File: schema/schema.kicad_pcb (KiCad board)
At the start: 2 copper layers, 91.4 x 55.9 mm, 14 parts, among them J1 Conn_01x04_Male, J2 Conn_01x04_Male, J3 Conn_01x05_Male

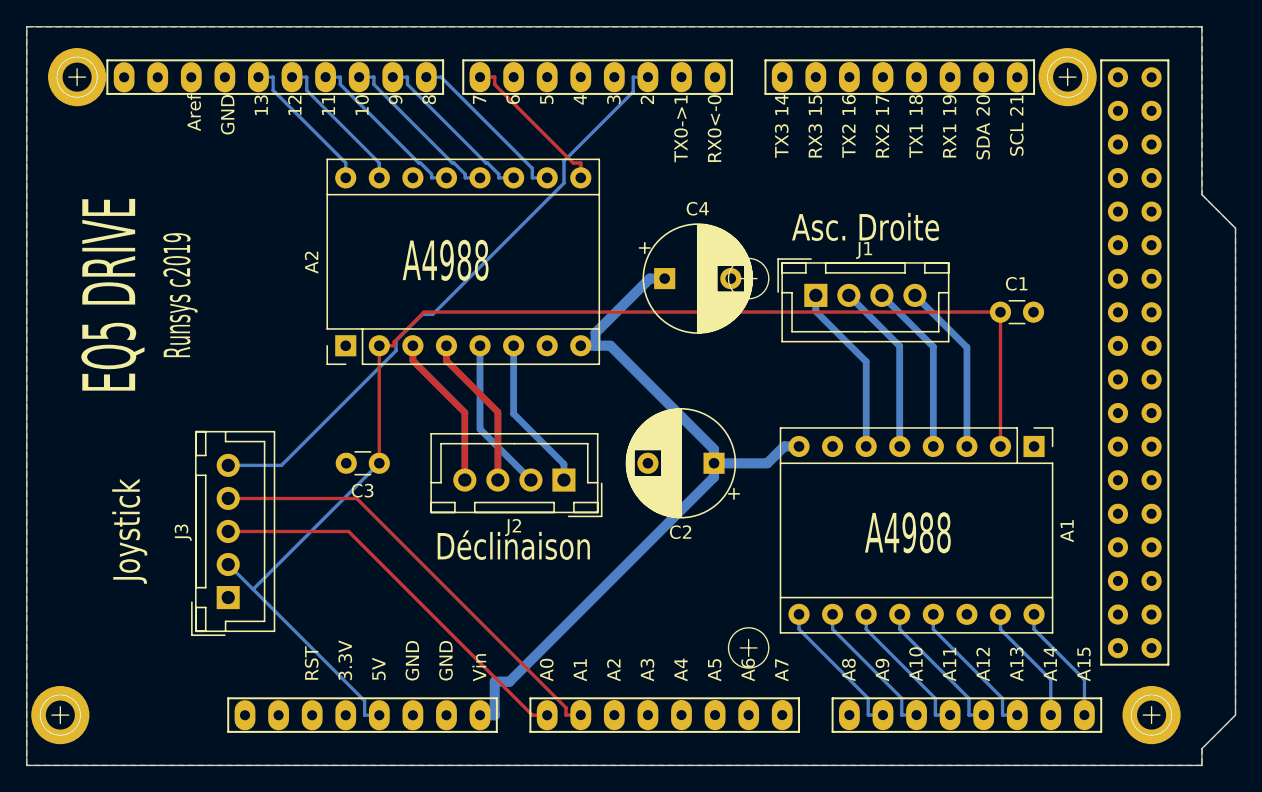
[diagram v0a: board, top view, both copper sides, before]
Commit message: Ajout Logo telescope
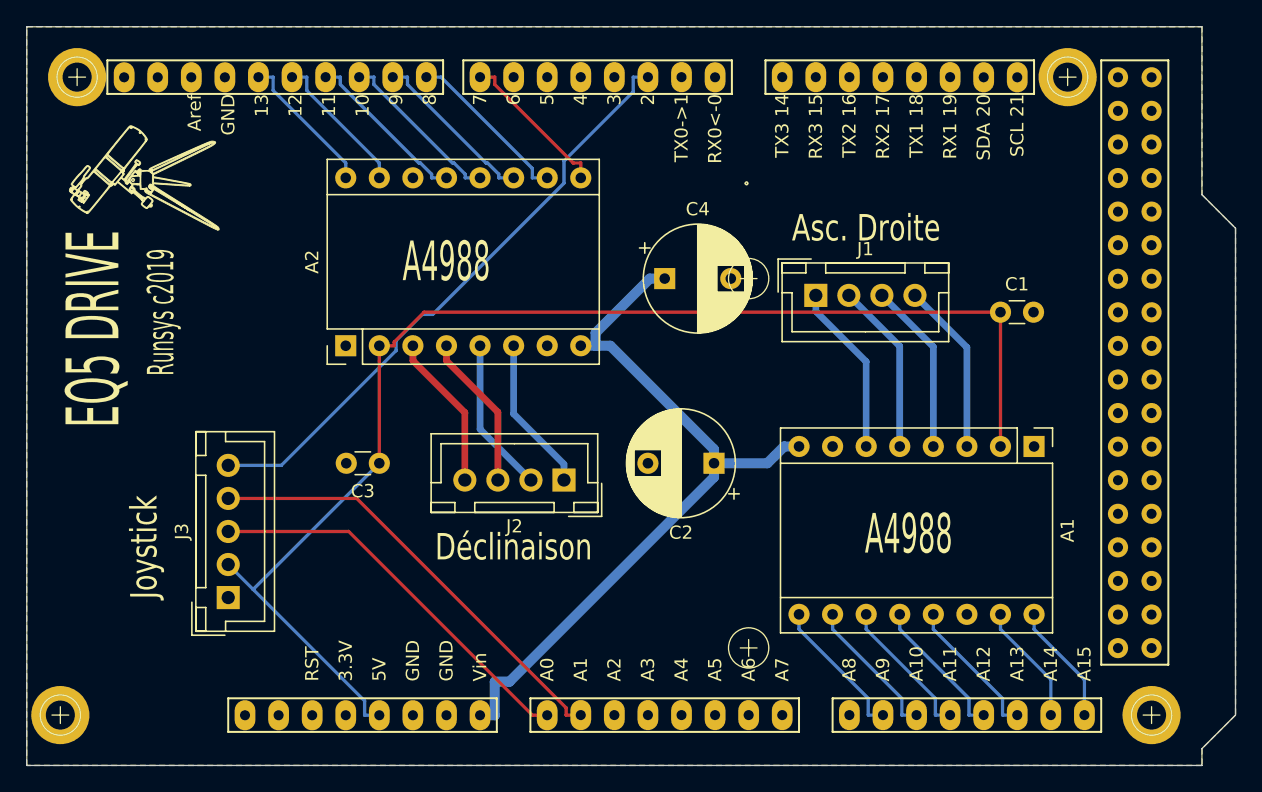
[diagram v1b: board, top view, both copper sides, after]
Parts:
- added G***: LOGO, logo:tele, F.Cu at (146.1, 74.9)
- added G***: LOGO, logo:tele, F.Cu at (100.3, 73.7)

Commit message: Modifiction du condo de 100nF
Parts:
- C1, C3: footprint Capacitors_THT:C_Disc_D3.0mm_W1.6mm_P2.50mm -> Capacitor_THT:C_Disc_D5.1mm_W3.2mm_P5.00mm
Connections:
- SH1 pad GND3: Net-(SH1-PadGND3) -> GND

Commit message: Modificatin pour la 3D sur les connexteurs JST
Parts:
- J1, J2: footprint Connectors_JST:JST_XH_B04B-XH-A_04x2.50mm_Straight -> Connector_JST:JST_XH_B4B-XH-A_1x04_P2.50mm_Vertical
- J3: footprint Connectors_JST:JST_XH_B05B-XH-A_05x2.50mm_Straight -> Connector_JST:JST_XH_B5B-XH-A_1x05_P2.50mm_Vertical

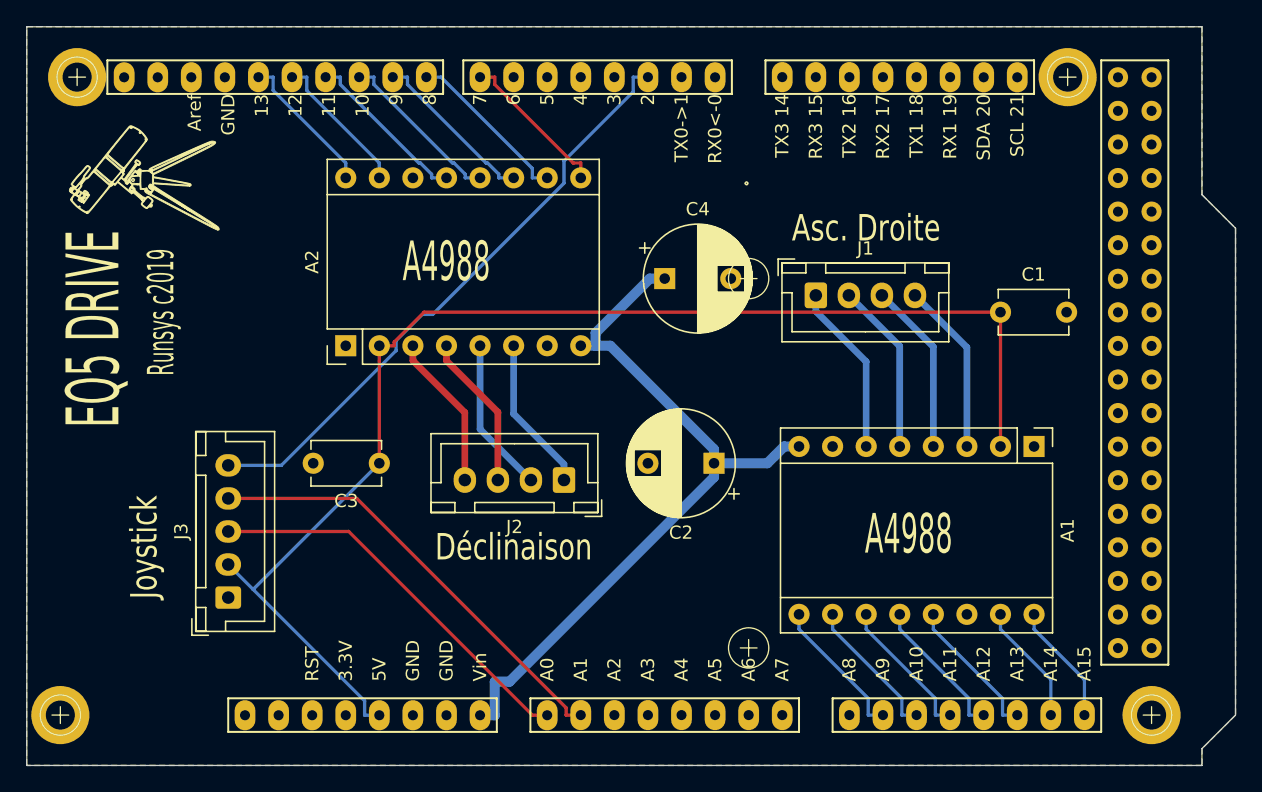
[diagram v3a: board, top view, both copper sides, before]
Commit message: Changement de taille des pistes 12V et 5V
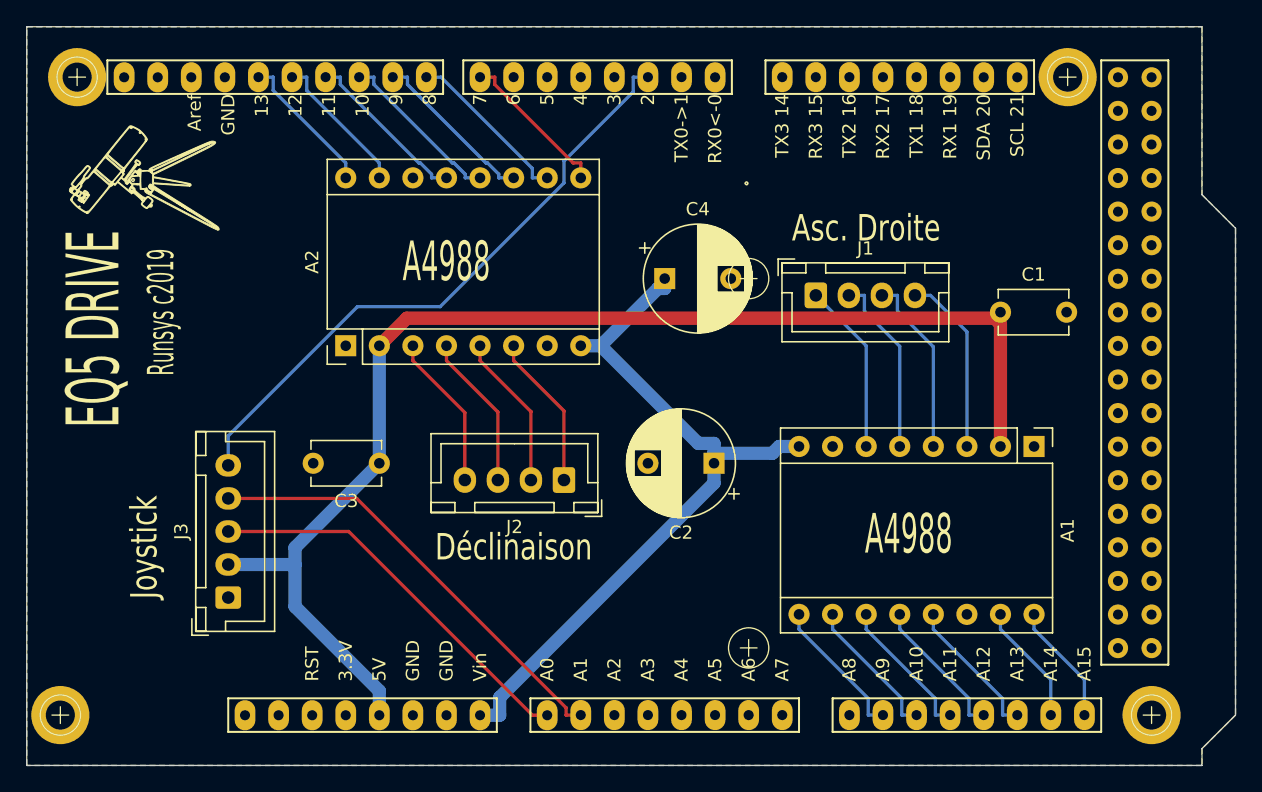
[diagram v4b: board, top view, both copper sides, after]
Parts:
- renumbered G*** to G0, G*** to G1, REF** to REF1, REF** to REF2, REF** to REF3
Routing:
- net +5V: track 97.5 -> 96.2 mm
- net +12V: track 56.9 -> 55.9 mm
- net Net-(J3-Pad5): track 46.0 -> 46.8 mm
- net Net-(A1-Pad5): track 13.0 -> 13.7 mm
- net Net-(A1-Pad4): track 13.0 -> 13.7 mm
- net Net-(A1-Pad3): track 13.1 -> 13.7 mm
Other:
- net class 12V added: clearance 0.2, trace_width 1, via_dia 0.8, via_drill 0.4
- net class 5V added: clearance 0.2, trace_width 1, via_dia 0.8, via_drill 0.4
